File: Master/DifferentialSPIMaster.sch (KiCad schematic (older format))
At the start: 42 parts, among them J1 Motor Encoder 0, J2 Conn_01x20, J3 Motor Encoder 0, U1 MAX14783ExS, U2 MAX14783ExS, U3 MAX14783ExS, U4 MAX14783ExS, U5 MAX14783ExS

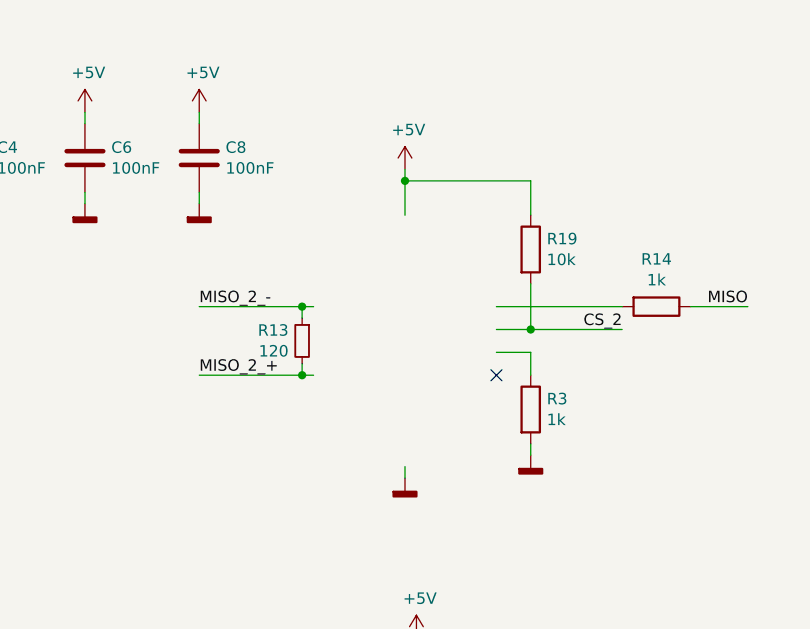
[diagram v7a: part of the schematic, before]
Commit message: Swap to MAX14783 on Master
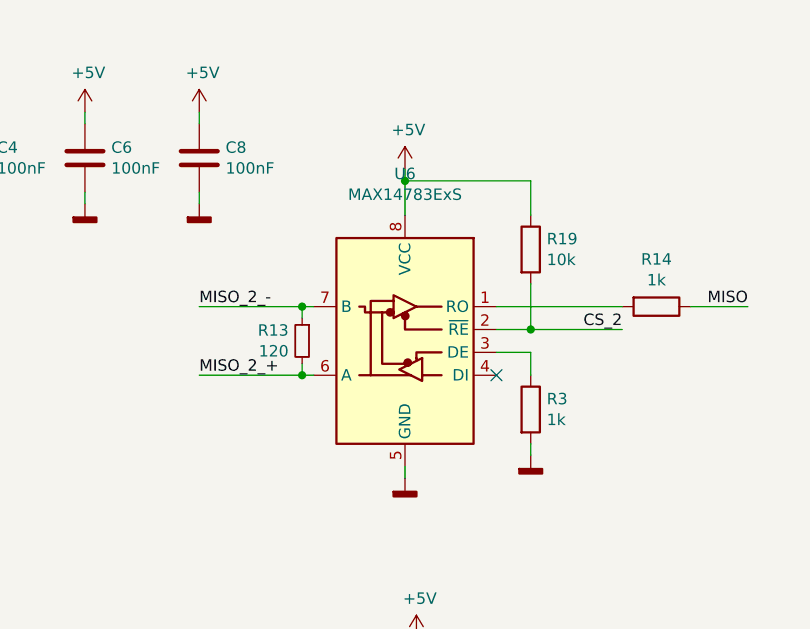
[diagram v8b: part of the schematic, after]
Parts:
- added U6: MAX14783ExS, Package_SO:SOIC-8_3.9x4.9mm_P1.27mm, symbol Interface_UART:MAX14783ExS
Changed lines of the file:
@@
+	-1   0    0    -1
+$EndComp
+$Comp
+L Interface_UART:MAX14783ExS U6
+U 1 1 5F1CA018
+P 6150 7300
+F 0 "U6" H 6150 7981 50  0000 C CNN
+F 1 "MAX14783ExS" H 6150 7890 50  0000 C CNN
+F 2 "Package_SO:SOIC-8_3.9x4.9mm_P1.27mm" H 6150 6400 50  0001 C CNN
+F 3 "https://datasheets.maximintegrated.com/en/ds/MAX14783E.pdf" H 6150 7350 50  0001 C CNN
+	1    6150 7300
 	-1   0    0    -1
 $EndComp
